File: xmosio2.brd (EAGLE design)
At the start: 116.8 x 55.2 mm, 103 parts, among them IC1 IDTQS3245QSOP20, IC2 IDTQS3245QSOP20, IC3 IDTQS3245QSOP20, IC4 IDTQS3245QSOP20, IC5 IDTQS3245QSOP20, U1 24 MHz Osc. (F535L-24), U2 USD-SOCKETNEW, X1 0446200002

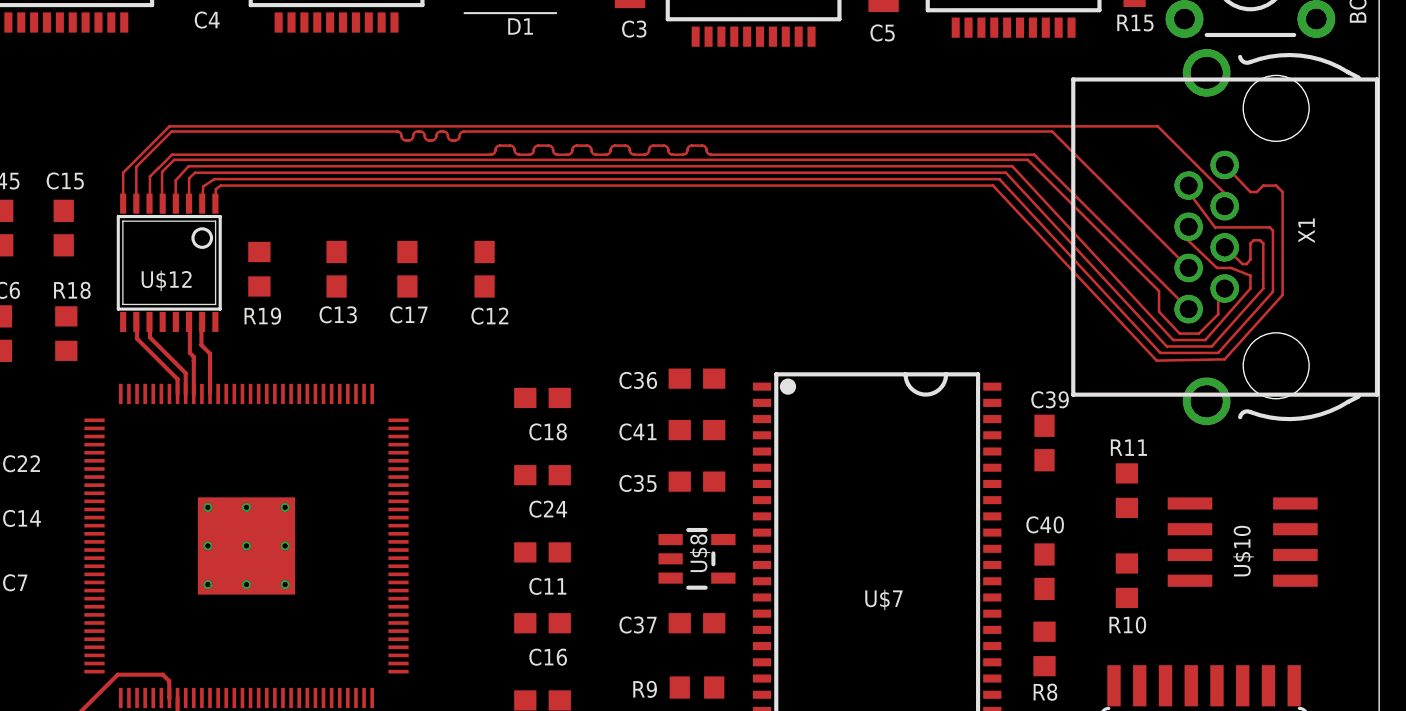
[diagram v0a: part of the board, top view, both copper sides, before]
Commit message: Trying to get the board to route with Seeed’s cheaper options. It routes fine at OSH-park, but they’re a bit more expensive…
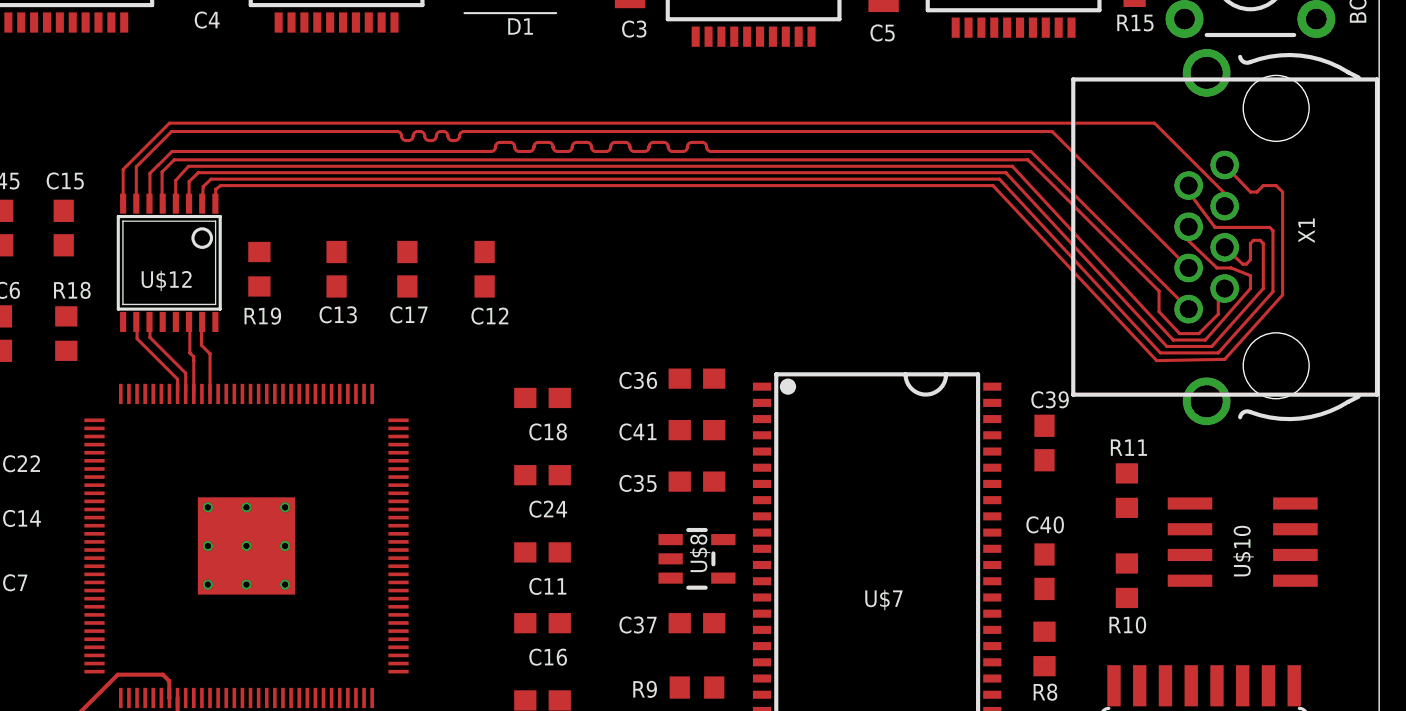
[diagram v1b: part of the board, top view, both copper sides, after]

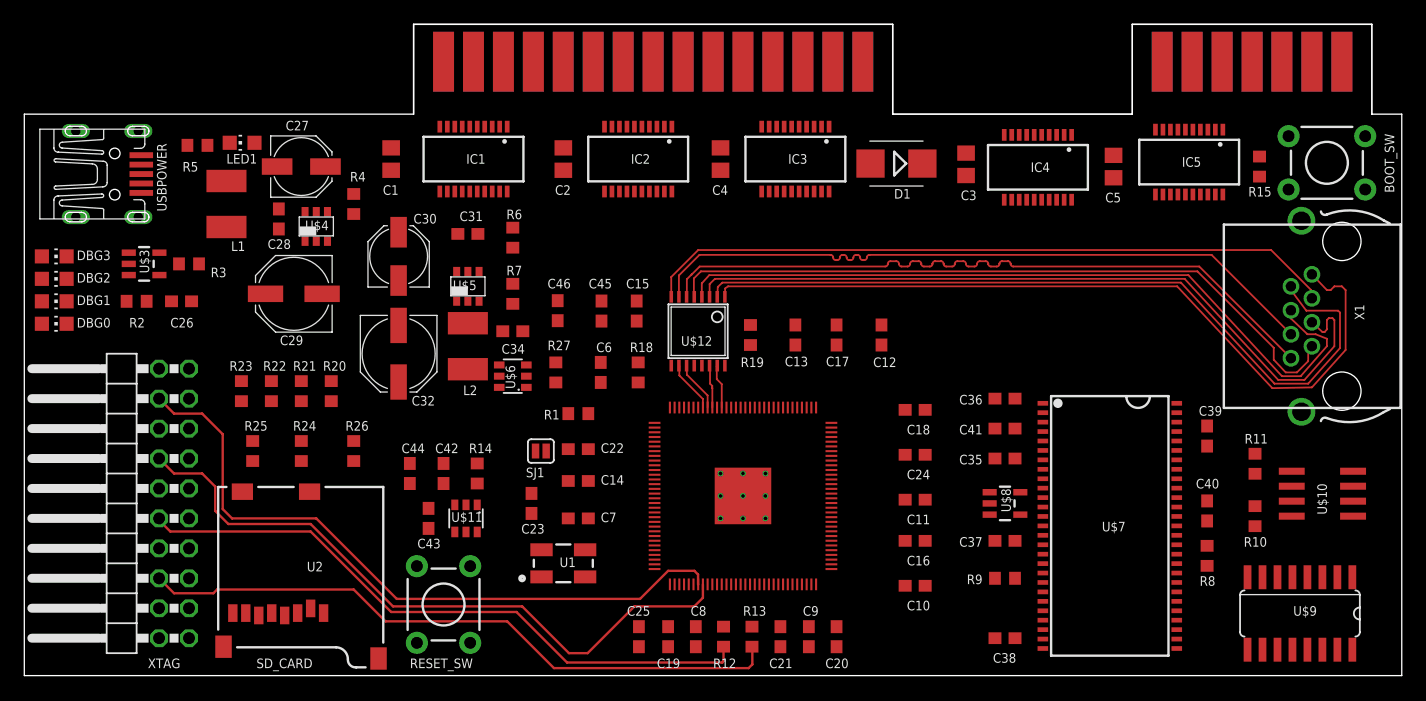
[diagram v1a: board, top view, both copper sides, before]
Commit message: - Add in zero-ohm resistor placeholders in case the drivers need 33R (like the JTAG interface does) - Better length matching, now sub-millimeter on all concerned traces - Move the boot-the-fallback-flash-image switch next to the reset switch - Move the decoupling capacitors closer to the XMOS chip - Move the SDRAM chip around to get better routing
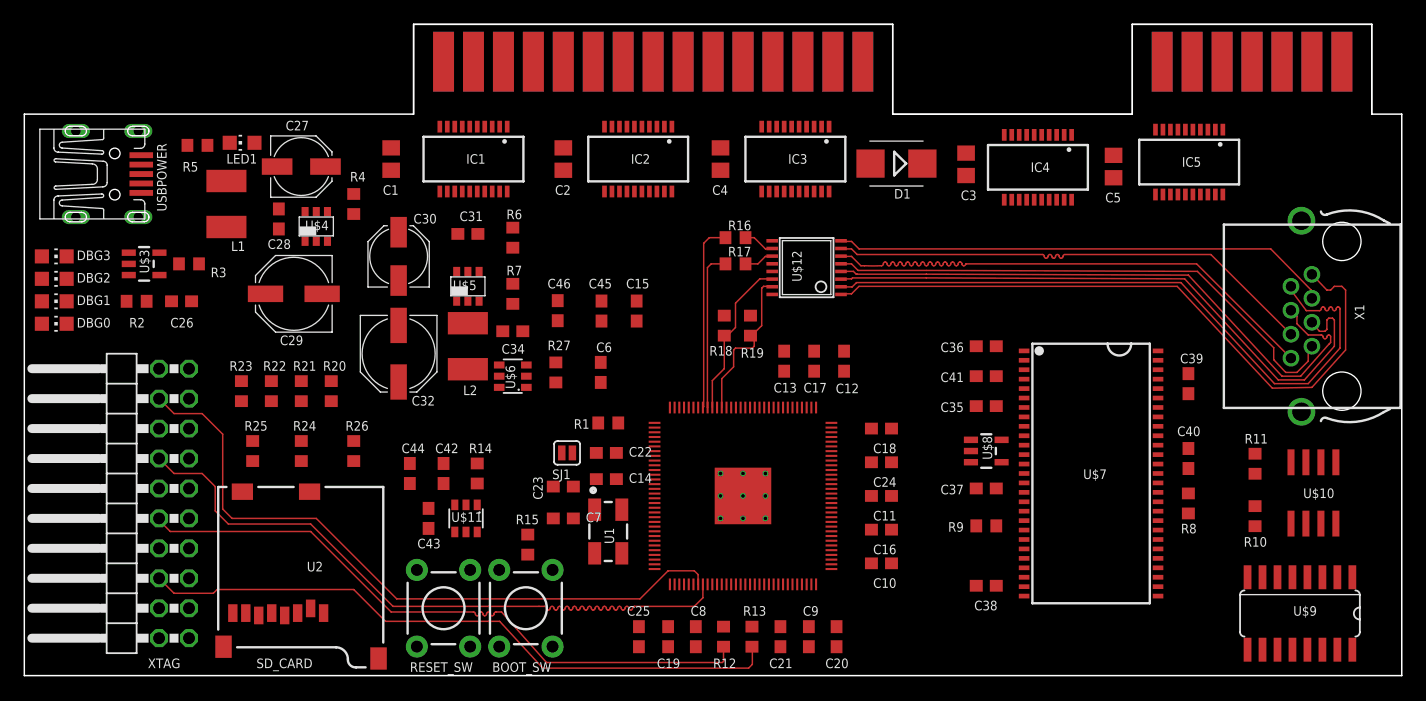
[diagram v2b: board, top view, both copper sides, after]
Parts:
- added R16, R17: 0R, rcl:R0603
- moved BOOT_SW 77.7 mm to (42.5, 5.71), turned to 270 degrees
- moved R15 69.9 mm to (42.7, 11.1), turned to 90 degrees
- moved U$12 10.7 mm to (66.4, 34.6), turned to 90 degrees
- moved R18 8.31 mm to (59.4, 29.7), turned to 270 degrees
- moved C35 4.72 mm to (81.6, 22.9)
- moved C36 4.72 mm to (81.6, 27.9)
- moved C37 4.72 mm to (81.6, 15.9)
- moved C38 4.72 mm to (81.6, 7.62)
- moved C41 4.72 mm to (81.6, 25.4)
- moved U$7 4.72 mm to (90.5, 17.1)
- moved U$8 4.72 mm to (81.6, 19.1)
- moved R9 4.72 mm to (81.6, 12.7)
- moved C39 4.72 mm to (98.7, 24.8)
- moved R8 4.72 mm to (98.7, 14.6)
- moved C40 4.72 mm to (98.7, 18.4)
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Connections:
- new net N$28: R17.1, U$2.88
- new net N$29: R16.1, U$2.89
- net LNK_OUT0: now also R17.2; no longer U$2.88
- net LNK_OUT1: now also R16.2; no longer U$2.89
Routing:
- net DOUT1_N: track 59.0 -> 42.4 mm
- net DOUT1_P: track 58.3 -> 42.0 mm
- net N$29: track 0.00 -> 16.0 mm
- net DOUT2_N: track 59.9 -> 45.8 mm
- net DOUT2_P: track 58.7 -> 44.8 mm
- net N$28: track 0.00 -> 13.5 mm
- net RIN2_P: track 64.8 -> 52.4 mm
- net RIN2_N: track 64.4 -> 52.1 mm
- net RIN1_N: track 67.3 -> 57.0 mm
- net RIN1_P: track 67.3 -> 57.0 mm
- net LNK_IN0: track 3.65 -> 13.8 mm
- net LNK_IN1: track 3.74 -> 13.6 mm
- net LNK_OUT0: track 4.29 -> 2.54 mm
- net LNK_OUT1: track 4.40 -> 2.67 mm
- net JTAG_UP0: track 54.4 -> 55.3 mm

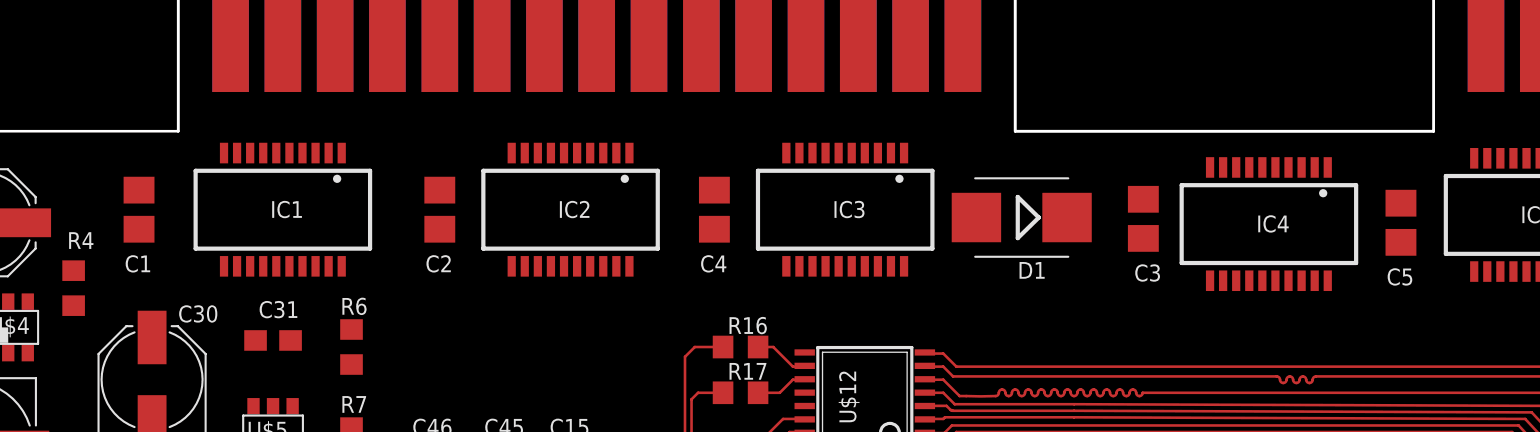
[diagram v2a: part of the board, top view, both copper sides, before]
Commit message: - Add some keepouts for easier soldering - Change the 0805 capacitors to be 0603
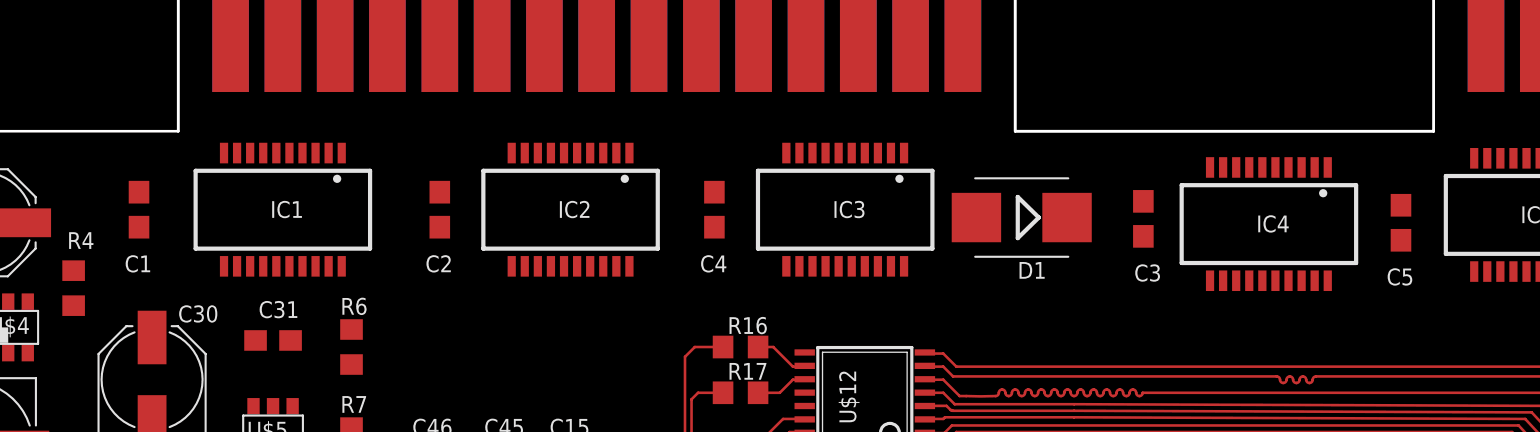
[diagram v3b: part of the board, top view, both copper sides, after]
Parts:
- C1, C2, C3, C4, C5: device rcl:C0805 -> rcl:C0603
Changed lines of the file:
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@@
 <attribute name="VALUE" x="101.411" y="44.8009" size="1.27" layer="27" rot="R180"/>
 </element>
-<element name="C5" library="rcl" package="C0805" value="100nF" x="92.3925" y="43.18" smashed="yes" rot="R90">
+<element name="C5" library="rcl" package="C0603" value="100nF" x="92.3925" y="43.18" smashed="yes" rot="R90">
 <attribute name="NAME" x="93.0275" y="40.9575" size="0.8128" layer="25" rot="R180"/>
 <attribute name="VALUE" x="94.9325" y="41.91" size="1.27" layer="27" rot="R90"/>
 </element>
-<element name="C1" library="rcl" package="C0805" value="100nF" x="31.115" y="43.815" smashed="yes" rot="R90">
+<element name="C1" library="rcl" package="C0603" value="100nF" x="31.115" y="43.815" smashed="yes" rot="R90">
 <attribute name="NAME" x="31.75" y="41.5925" size="0.8128" layer="25" rot="R180"/>
 <attribute name="VALUE" x="33.655" y="42.545" size="1.27" layer="27" rot="R90"/>
 </element>
-<element name="C2" library="rcl" package="C0805" value="100nF" x="45.72" y="43.815" smashed="yes" rot="R90">
+<element name="C2" library="rcl" package="C0603" value="100nF" x="45.72" y="43.815" smashed="yes" rot="R90">
 <attribute name="NAME" x="46.355" y="41.5925" size="0.8128" layer="25" rot="R180"/>
 <attribute name="VALUE" x="48.26" y="42.545" size="1.27" layer="27" rot="R90"/>
 </element>
-<element name="C3" library="rcl" package="C0805" value="100nF" x="79.883" y="43.3705" smashed="yes" rot="R90">
+<element name="C3" library="rcl" package="C0603" value="100nF" x="79.883" y="43.3705" smashed="yes" rot="R90">
 <attribute name="NAME" x="80.772" y="41.148" size="0.8128" layer="25" rot="R180"/>
 <attribute name="VALUE" x="82.423" y="42.1005" size="1.27" layer="27" rot="R90"/>
 </element>
-<element name="C4" library="rcl" package="C0805" value="100nF" x="59.055" y="43.815" smashed="yes" rot="R90">
+<element name="C4" library="rcl" package="C0603" value="100nF" x="59.055" y="43.815" smashed="yes" rot="R90">
 <attribute name="NAME" x="59.69" y="41.5925" size="0.8128" layer="25" rot="R180"/>
 <attribute name="VALUE" x="61.595" y="42.545" size="1.27" layer="27" rot="R90"/>
@@
 <wire x1="23.815" y1="36.85" x2="25.26" y2="32.385" width="0" layer="19" extent="1-1"/>
 <wire x1="27.94" y1="40.855" x2="23.815" y2="36.85" width="0" layer="19" extent="1-1"/>
-<wire x1="31.115" y1="44.765" x2="27.94" y2="40.855" width="0" layer="19" extent="1-1"/>
-<wire x1="35.242" y1="46.565" x2="31.115" y2="44.765" width="0" layer="19" extent="1-1"/>
+<wire x1="31.115" y1="44.665" x2="27.94" y2="40.855" width="0" layer="19" extent="1-1"/>
+<wire x1="35.242" y1="46.565" x2="31.115" y2="44.665" width="0" layer="19" extent="1-1"/>
 <wire x1="38.1" y1="52.07" x2="35.242" y2="46.565" width="0" layer="19" extent="1-1"/>
 <wire x1="21.445" y1="43.18" x2="23.815" y2="36.85" width="0" layer="19" extent="1-1"/>
@@
 <wire x1="67.628" y1="41.065" x2="63.4397" y2="36.8825" width="0" layer="19" extent="1-1"/>
 <wire x1="62.547" y1="46.565" x2="67.628" y2="41.065" width="0" layer="19" extent="1-1"/>
-<wire x1="59.055" y1="44.765" x2="62.547" y2="46.565" width="0" layer="19" extent="1-1"/>
-<wire x1="54.293" y1="41.065" x2="59.055" y2="44.765" width="0" layer="19" extent="1-1"/>
+<wire x1="59.055" y1="44.665" x2="62.547" y2="46.565" width="0" layer="19" extent="1-1"/>
+<wire x1="54.293" y1="41.065" x2="59.055" y2="44.665" width="0" layer="19" extent="1-1"/>
 <wire x1="49.212" y1="46.565" x2="54.293" y2="41.065" width="0" layer="19" extent="1-1"/>
-<wire x1="45.72" y1="44.765" x2="49.212" y2="46.565" width="0" layer="19" extent="1-1"/>
-<wire x1="40.323" y1="41.065" x2="45.72" y2="44.765" width="0" layer="19" extent="1-1"/>
+<wire x1="45.72" y1="44.665" x2="49.212" y2="46.565" width="0" layer="19" extent="1-1"/>
+<wire x1="40.323" y1="41.065" x2="45.72" y2="44.665" width="0" layer="19" extent="1-1"/>
 <wire x1="101.029" y1="40.811" x2="108.331" y2="38.5826" width="0" layer="19" extent="1-1"/>
 <wire x1="95.948" y1="46.311" x2="101.029" y2="40.811" width="0" layer="19" extent="1-1"/>
-<wire x1="92.3925" y1="44.13" x2="95.948" y2="46.311" width="0" layer="19" extent="1-1"/>
-<wire x1="88.202" y1="40.3665" x2="92.3925" y2="44.13" width="0" layer="19" extent="1-1"/>
+<wire x1="92.3925" y1="44.03" x2="95.948" y2="46.311" width="0" layer="19" extent="1-1"/>
+<wire x1="88.202" y1="40.3665" x2="92.3925" y2="44.03" width="0" layer="19" extent="1-1"/>
 <wire x1="83.121" y1="45.8665" x2="88.202" y2="40.3665" width="0" layer="19" extent="1-1"/>
-<wire x1="79.883" y1="44.3205" x2="83.121" y2="45.8665" width="0" layer="19" extent="1-1"/>
+<wire x1="79.883" y1="44.2205" x2="83.121" y2="45.8665" width="0" layer="19" extent="1-1"/>
 <wire x1="73.5575" y1="20.955" x2="69.5325" y2="27.52" width="0" layer="19" extent="1-1"/>
 <wire x1="73.5575" y1="18.0975" x2="73.5575" y2="20.955" width="0" layer="19" extent="1-1"/>
@@
 <contactref element="C4" pad="1"/>
 <contactref element="IC5" pad="20"/>
-<wire x1="92.3925" y1="42.23" x2="101.664" y2="40.811" width="0" layer="19" extent="1-1"/>
-<wire x1="88.837" y1="40.3665" x2="92.3925" y2="42.23" width="0" layer="19" extent="1-1"/>
-<wire x1="79.883" y1="42.4205" x2="88.837" y2="40.3665" width="0" layer="19" extent="1-1"/>
-<wire x1="76.1775" y1="43.434" x2="79.883" y2="42.4205" width="0" layer="19" extent="1-1"/>
+<wire x1="92.3925" y1="42.33" x2="101.664" y2="40.811" width="0" layer="19" extent="1-1"/>
+<wire x1="88.837" y1="40.3665" x2="92.3925" y2="42.33" width="0" layer="19" extent="1-1"/>
+<wire x1="79.883" y1="42.5205" x2="88.837" y2="40.3665" width="0" layer="19" extent="1-1"/>
+<wire x1="76.1775" y1="43.434" x2="79.883" y2="42.5205" width="0" layer="19" extent="1-1"/>
 <wire x1="68.263" y1="41.065" x2="76.1775" y2="43.434" width="0" layer="19" extent="1-1"/>
-<wire x1="59.055" y1="42.865" x2="68.263" y2="41.065" width="0" layer="19" extent="1-1"/>
-<wire x1="54.928" y1="41.065" x2="59.055" y2="42.865" width="0" layer="19" extent="1-1"/>
-<wire x1="45.72" y1="42.865" x2="54.928" y2="41.065" width="0" layer="19" extent="1-1"/>
-<wire x1="40.958" y1="41.065" x2="45.72" y2="42.865" width="0" layer="19" extent="1-1"/>
-<wire x1="31.115" y1="42.865" x2="40.958" y2="41.065" width="0" layer="19" extent="1-1"/>
+<wire x1="59.055" y1="42.965" x2="68.263" y2="41.065" width="0" layer="19" extent="1-1"/>
+<wire x1="54.928" y1="41.065" x2="59.055" y2="42.965" width="0" layer="19" extent="1-1"/>
+<wire x1="45.72" y1="42.965" x2="54.928" y2="41.065" width="0" layer="19" extent="1-1"/>
+<wire x1="40.958" y1="41.065" x2="45.72" y2="42.965" width="0" layer="19" extent="1-1"/>
+<wire x1="31.115" y1="42.965" x2="40.958" y2="41.065" width="0" layer="19" extent="1-1"/>
 </signal>
 <signal name="N$10">
